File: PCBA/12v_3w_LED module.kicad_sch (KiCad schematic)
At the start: 1 part

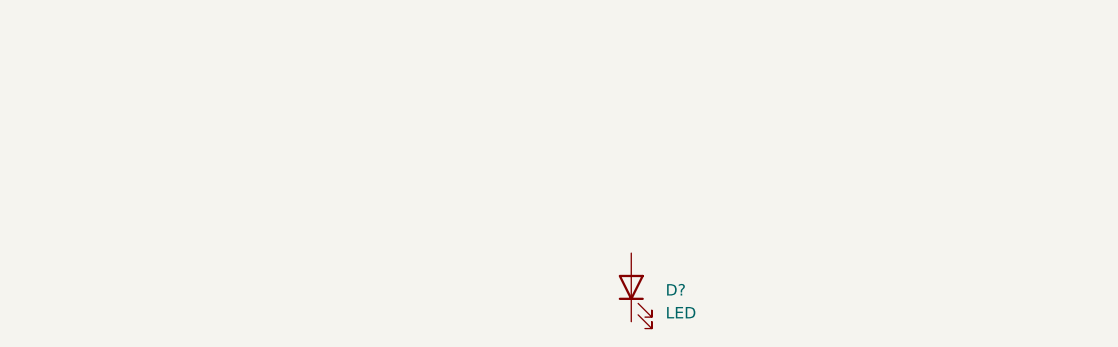
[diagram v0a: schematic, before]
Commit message: creacion esquematico e inicio de PCB
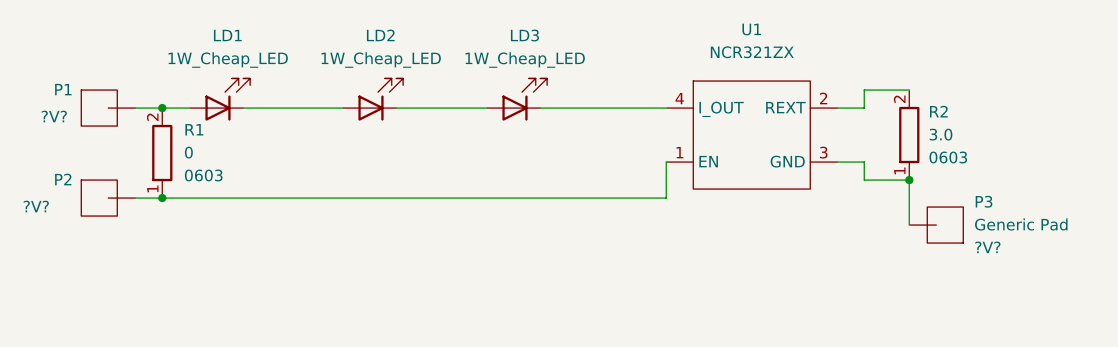
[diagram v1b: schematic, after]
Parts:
- removed D?: LED, symbol Device:LED
- added LD1, LD2, LD3: 1W_Cheap_LED, Herranz-HighpowerLED:1W_cheap_LED, symbol Herranz - HighPowerLED:1W_Cheap_LED
- added P1, P2, P3: Generic Pad, Herranz - Various:Generic Pad, symbol Herranz - Various:Generic Pad
- added R1: 0, Resistor_SMD:R_0603_1608Metric, symbol Herranz - Resistors (0603):0
- added R2: 3.0, Resistor_SMD:R_0603_1608Metric, symbol Herranz - Resistors (0603):3.0
- added U1: NCR321ZX, Herranz - LED controller:SOT230P700X180-4N, symbol Herranz - LED controller:NCR321ZX
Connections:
- new net: P2.1, R1.1, U1.1 (EN)
- new net: R2.2, U1.2 (REXT)
- new net: P3.1, R2.1, U1.3 (GND)
- new net: LD3.2 (K), U1.4 (I_OUT)
- new net: LD2.2 (K), LD3.1 (A)
- new net: LD1.1 (A), P1.1, R1.2
- new net: LD1.2 (K), LD2.1 (A)
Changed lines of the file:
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@@
 (kicad_sch (version 20211123) (generator eeschema)
-  (paper "A4")
-  (symbol (lib_id "Device:LED") (at 118.11 74.93 90) (unit 1)
-    (in_bom yes) (on_board yes) (fields_autoplaced)
-    (property "Reference" "D?" (id 0) (at 121.92 75.2474 90)
-      (effects (font (size 1.27 1.27)) (justify right))
-    )
-    (property "Value" "LED" (id 1) (at 121.92 77.7874 90)
-      (effects (font (size 1.27 1.27)) (justify right))
-    )
-    (property "Footprint" "" (id 2) (at 118.11 74.93 0)
-      (effects (font (size 1.27 1.27)) hide)
-    )
-    (property "Datasheet" "~" (id 3) (at 118.11 74.93 0)
-      (effects (font (size 1.27 1.27)) hide)
-    )
-    (pin "1")
-    (pin "2")
+  (paper "A5")
+  (junction (at 149 63) (diameter 0) (color 0 0 0 0)
+  )
+  (junction (at 66 55) (diameter 0) (color 0 0 0 0)
+  )
+  (junction (at 66 65) (diameter 0) (color 0 0 0 0)
+  )
+  (wire (pts (xy 144 61) (xy 144 63))
+    (stroke (width 0) (type default) (color 0 0 0 0))
+  )
+  (wire (pts (xy 144 63) (xy 149 63))
+    (stroke (width 0) (type default) (color 0 0 0 0))
+  )
+  (wire (pts (xy 141 55) (xy 144 55))
+    (stroke (width 0) (type default) (color 0 0 0 0))
+  )
+  (wire (pts (xy 92 55) (xy 102 55))
+    (stroke (width 0) (type default) (color 0 0 0 0))
+  )
+  (wire (pts (xy 66 65) (xy 122 65))
+    (stroke (width 0) (type default) (color 0 0 0 0))
+  )
+  (wire (pts (xy 122 61) (xy 122 65))
+    (stroke (width 0) (type default) (color 0 0 0 0))
+  )
+  (wire (pts (xy 141 61) (xy 144 61))
+    (stroke (width 0) (type default) (color 0 0 0 0))
+  )
+  (wire (pts (xy 66 55) (xy 69 55))
+    (stroke (width 0) (type default) (color 0 0 0 0))
+  )
+  (wire (pts (xy 144 53) (xy 149 53))
+    (stroke (width 0) (type default) (color 0 0 0 0))
+  )
+  (wire (pts (xy 144 55) (xy 144 53))
+    (stroke (width 0) (type default) (color 0 0 0 0))
+  )
+  (wire (pts (xy 63 55) (xy 66 55))
+    (stroke (width 0) (type default) (color 0 0 0 0))
+  )
+  (wire (pts (xy 108 55) (xy 122 55))
+    (stroke (width 0) (type default) (color 0 0 0 0))
+  )
+  (wire (pts (xy 75 55) (xy 86 55))
+    (stroke (width 0) (type default) (color 0 0 0 0))
+  )
+  (wire (pts (xy 149 63) (xy 149 68))
+    (stroke (width 0) (type default) (color 0 0 0 0))
+  )
+  (wire (pts (xy 63 65) (xy 66 65))
+    (stroke (width 0) (type default) (color 0 0 0 0))
+  )
+  (symbol (lib_id "Herranz - LED controller:NCR321ZX") (at 132 50 0) (unit 1)
+    (in_bom yes) (on_board yes) (fields_autoplaced)
+    (property "Reference" "U1" (id 0) (at 131.5 46.31 0))
+    (property "Value" "NCR321ZX" (id 1) (at 131.5 48.85 0))
+    (property "Footprint" "Herranz - LED controller:SOT230P700X180-4N" (id 2) (at 132 50 0)
+      (effects (font (size 1.27 1.27)) hide)
+    )
+    (property "Datasheet" "" (id 3) (at 132 50 0)
+      (effects (font (size 1.27 1.27)) hide)
+    )
+    (pin "1")
+    (pin "2")
+    (pin "3")
+    (pin "4")
+  )
+  (symbol (lib_id "Herranz - HighPowerLED:1W_Cheap_LED") (at 111 52 0) (unit 1)
+    (in_bom yes) (on_board yes) (fields_autoplaced)
+    (property "Reference" "LD3" (id 0) (at 106.2775 46.99 0))
+    (property "Value" "1W_Cheap_LED" (id 1) (at 106.2775 49.53 0))
+    (property "Footprint" "Herranz-HighpowerLED:1W_cheap_LED" (id 2) (at 105 61 0)
+      (effects (font (size 1.27 1.27)) hide)
+    )
+    (property "Datasheet" "" (id 3) (at 105 61 0)
+      (effects (font (size 1.27 1.27)) hide)
+    )
+    (pin "1")
+    (pin "2")
+  )
+  (symbol (lib_id "Herranz - Various:Generic Pad") (at 59 61 0) (unit 1)
+    (in_bom yes) (on_board yes)
+    (property "Reference" "P2" (id 0) (at 55 63 0))
+    (property "Value" "Generic Pad" (id 1) (at 50 65 0)
+      (effects (font (size 1.27 1.27)) hide)
+    )
+    (property "Footprint" "Herranz - Various:Generic Pad" (id 2) (at 59 59 0)
+      (effects (font (size 1.27 1.27)) hide)
+    )
+    (property "Datasheet" "" (id 3) (at 59 61 0)
+      (effects (font (size 1.27 1.27)) hide)
+    )
+    (property "Voltage" "?V?" (id 4) (at 52 66 0))
+    (pin "1")
+  )
+  (symbol (lib_id "Herranz - HighPowerLED:1W_Cheap_LED") (at 78 52 0) (unit 1)
+    (in_bom yes) (on_board yes) (fields_autoplaced)
+    (property "Reference" "LD1" (id 0) (at 73.2775 46.99 0))
+    (property "Value" "1W_Cheap_LED" (id 1) (at 73.2775 49.53 0))
+    (property "Footprint" "Herranz-HighpowerLED:1W_cheap_LED" (id 2) (at 72 61 0)
+      (effects (font (size 1.27 1.27)) hide)
+    )
+    (property "Datasheet" "" (id 3) (at 72 61 0)
+      (effects (font (size 1.27 1.27)) hide)
+    )
+    (pin "1")
+    (pin "2")
+  )
+  (symbol (lib_id "Herranz - HighPowerLED:1W_Cheap_LED") (at 95 52 0) (unit 1)
+    (in_bom yes) (on_board yes) (fields_autoplaced)
+    (property "Reference" "LD2" (id 0) (at 90.2775 46.99 0))
+    (property "Value" "1W_Cheap_LED" (id 1) (at 90.2775 49.53 0))
+    (property "Footprint" "Herranz-HighpowerLED:1W_cheap_LED" (id 2) (at 89 61 0)
+      (effects (font (size 1.27 1.27)) hide)
+    )
+    (property "Datasheet" "" (id 3) (at 89 61 0)
+      (effects (font (size 1.27 1.27)) hide)
+    )
+    (pin "1")
+    (pin "2")
+  )
+  (symbol (lib_id "Herranz - Resistors (0603):3.0") (at 148 58 90) (unit 1)
+    (in_bom yes) (on_board yes) (fields_autoplaced)
+    (property "Reference" "R2" (id 0) (at 151.13 55.4599 90)
+      (effects (font (size 1.27 1.27)) (justify right))
+    )
+    (property "Value" "3.0" (id 1) (at 151.13 57.9999 90)
+      (effects (font (size 1.27 1.27)) (justify right))
+    )
+    (property "Footprint" "Resistor_SMD:R_0603_1608Metric" (id 2) (at 145 58 0)
+      (effects (font (size 1.27 1.27)) hide)
+    )
+    (property "Datasheet" "" (id 3) (at 148 58 0)
+      (effects (font (size 1.27 1.27)) hide)
+    )
+    (property "Size" "0603" (id 4) (at 151.13 60.5399 90)
+      (effects (font (size 1.27 1.27)) (justify right))
+    )
+    (pin "1")
+    (pin "2")
+  )
+  (symbol (lib_id "Herranz - Various:Generic Pad") (at 153 72 180) (unit 1)
+    (in_bom yes) (on_board yes) (fields_autoplaced)
+    (property "Reference" "P3" (id 0) (at 156.21 65.4599 0)
+      (effects (font (size 1.27 1.27)) (justify right))
+    )
+    (property "Value" "Generic Pad" (id 1) (at 156.21 67.9999 0)
+      (effects (font (size 1.27 1.27)) (justify right))
+    )
+    (property "Footprint" "Herranz - Various:Generic Pad" (id 2) (at 153 74 0)
+      (effects (font (size 1.27 1.27)) hide)
+    )
+    (property "Datasheet" "" (id 3) (at 153 72 0)
+      (effects (font (size 1.27 1.27)) hide)
+    )
+    (property "Voltage" "?V?" (id 4) (at 156.21 70.5399 0)
+      (effects (font (size 1.27 1.27)) (justify right))
+    )
+    (pin "1")
+  )
+  (symbol (lib_id "Herranz - Resistors (0603):0") (at 65 60 90) (unit 1)
+    (in_bom no) (on_board yes) (fields_autoplaced)
+    (property "Reference" "R1" (id 0) (at 68.4 57.4599 90)
+      (effects (font (size 1.27 1.27)) (justify right))
+    )
+    (property "Value" "0" (id 1) (at 68.4 59.9999 90)
+      (effects (font (size 1.27 1.27)) (justify right))
+    )
+    (property "Footprint" "Resistor_SMD:R_0603_1608Metric" (id 2) (at 62 60 0)
+      (effects (font (size 1.27 1.27)) hide)
+    )
+    (property "Datasheet" "" (id 3) (at 65 60 0)
+      (effects (font (size 1.27 1.27)) hide)
+    )
+    (property "Size" "0603" (id 4) (at 68.4 62.5399 90)
+      (effects (font (size 1.27 1.27)) (justify right))
+    )
+    (pin "1")
+    (pin "2")
+  )
+  (symbol (lib_id "Herranz - Various:Generic Pad") (at 59 51 0) (unit 1)
+    (in_bom yes) (on_board yes)
+    (property "Reference" "P1" (id 0) (at 55 53 0))
+    (property "Value" "Generic Pad" (id 1) (at 49 54 0)
+      (effects (font (size 1.27 1.27)) hide)
+    )
+    (property "Footprint" "Herranz - Various:Generic Pad" (id 2) (at 59 49 0)
+      (effects (font (size 1.27 1.27)) hide)
+    )
+    (property "Datasheet" "" (id 3) (at 59 51 0)
+      (effects (font (size 1.27 1.27)) hide)
+    )
+    (property "Voltage" "?V?" (id 4) (at 54 56 0))
+    (pin "1")
   )
   (sheet_instances
@@
   )
   (symbol_instances
-    (path "/4f66b314-0f62-4fb6-8c3c-f9c6a75cd3ec"
-      (reference "D?") (unit 1) (value "LED") (footprint "")
-    )
-  )
+    (path "/8a2faef4-cb1d-4e12-b861-3b3f8f3b8854"
+      (reference "LD1") (unit 1) (value "1W_Cheap_LED") (footprint "Herranz-HighpowerLED:1W_cheap_LED")
+    )
+    (path "/b8cc6224-2f81-46b6-a77a-773baaf2b6d0"
+      (reference "LD2") (unit 1) (value "1W_Cheap_LED") (footprint "Herranz-HighpowerLED:1W_cheap_LED")
+    )
+    (path "/15758638-c691-4c62-8b08-61d87b1ccc27"
+      (reference "LD3") (unit 1) (value "1W_Cheap_LED") (footprint "Herranz-HighpowerLED:1W_cheap_LED")
+    )
+    (path "/f400498f-618e-4b69-883c-9d983c10fdf8"
+      (reference "P1") (unit 1) (value "Generic Pad") (footprint "Herranz - Various:Generic Pad")
+    )
+    (path "/28474a48-9769-4c21-9240-855c52d9bc69"
+      (reference "P2") (unit 1) (value "Generic Pad") (footprint "Herranz - Various:Generic Pad")
+    )
+    (path "/db0b5805-bf6e-4a66-8b98-d907945d0655"
+      (reference "P3") (unit 1) (value "Generic Pad") (footprint "Herranz - Various:Generic Pad")
+    )
+    (path "/e44ed356-8143-4d95-bf6d-93364da9becd"
+      (reference "R1") (unit 1) (value "0") (footprint "Resistor_SMD:R_0603_1608Metric")
+    )
+    (path "/c050f93b-99fc-4403-acb9-bb7815e175e0"
+      (reference "R2") (unit 1) (value "3.0") (footprint "Resistor_SMD:R_0603_1608Metric")
+    )
+    (path "/10d05a43-64b9-4ab0-b7ea-9ec56a493db7"
+      (reference "U1") (unit 1) (value "NCR321ZX") (footprint "Herranz - LED controller:SOT230P700X180-4N")
+    )
+  )
